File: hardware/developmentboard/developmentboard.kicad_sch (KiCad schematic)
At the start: 38 parts, among them J1 SPI Header, J2 Power Header, J3 Hall Effect Header, U1 ADS7960, U10 DRV5053, U11 DRV5053, U12 DRV5053, U13 DRV5053, U14 AP2138N-2.5, U15 REF5025AD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

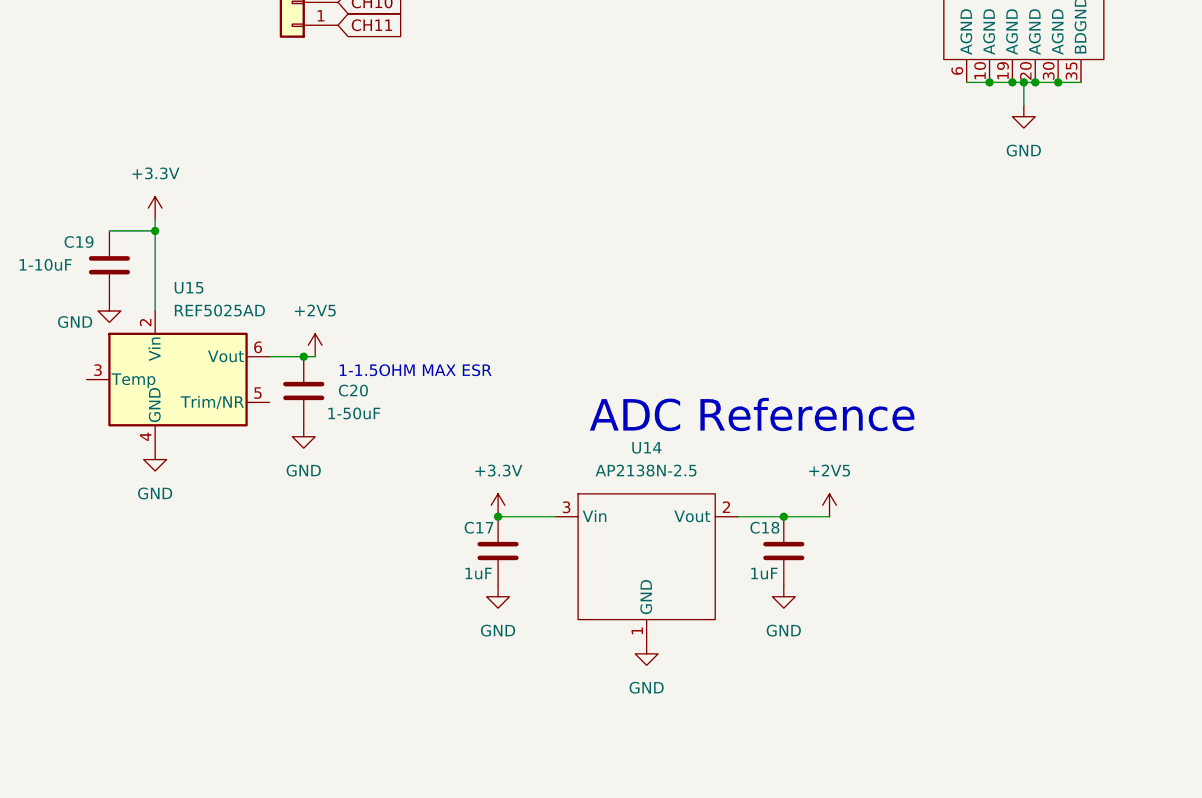
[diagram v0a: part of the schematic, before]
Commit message: added reference IC to PCB, removed LDO
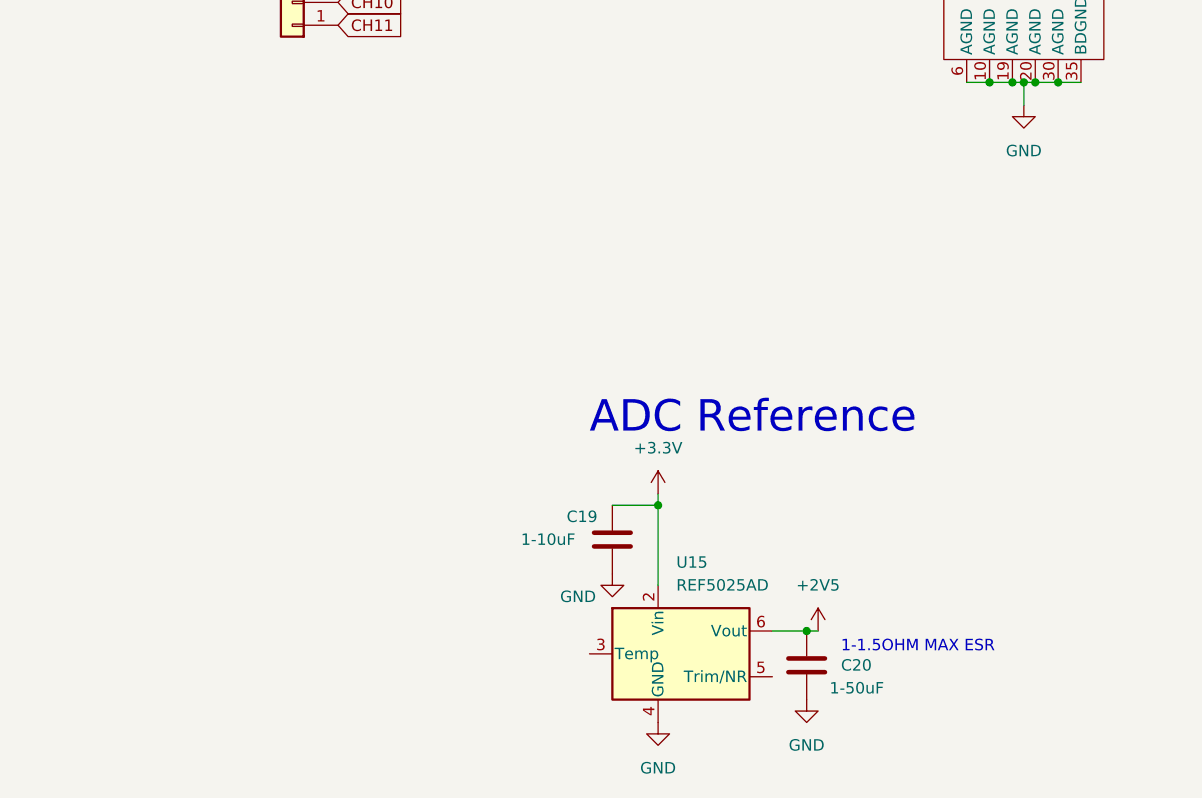
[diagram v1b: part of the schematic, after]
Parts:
- removed C17, C18: 1uF, Capacitor_SMD:C_0603_1608Metric, symbol Device:C
- removed U14: AP2138N-2.5, Package_TO_SOT_SMD:TSOT-23, symbol ece_capstone:AP2138N-2.5
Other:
- moved on the sheet: C19, C20, U15

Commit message: finalized reference IC pcb stuffs - added footprints for bypass caps
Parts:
- C19, C20: footprint (none) -> Capacitor_SMD:C_0603_1608Metric
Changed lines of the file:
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@@
       (effects (font (size 1.27 1.27)) (justify left))
     )
-    (property "Footprint" "" (id 2) (at 108.9152 182.88 0)
+    (property "Footprint" "Capacitor_SMD:C_0603_1608Metric" (id 2) (at 108.9152 182.88 0)
       (effects (font (size 1.27 1.27)) hide)
     )
@@
       (effects (font (size 1.27 1.27)) (justify left))
     )
-    (property "Footprint" "" (id 2) (at 87.3252 168.91 0)
+    (property "Footprint" "Capacitor_SMD:C_0603_1608Metric" (id 2) (at 87.3252 168.91 0)
       (effects (font (size 1.27 1.27)) hide)
     )
@@
     )
     (path "/f6e9c87b-24f6-4288-9254-c44dca53d4ee"
-      (reference "C19") (unit 1) (value "1-10uF") (footprint "")
+      (reference "C19") (unit 1) (value "1-10uF") (footprint "Capacitor_SMD:C_0603_1608Metric")
     )
     (path "/b545a864-3c9e-4894-8a24-dc831b2fea0f"
-      (reference "C20") (unit 1) (value "1-50uF") (footprint "")
+      (reference "C20") (unit 1) (value "1-50uF") (footprint "Capacitor_SMD:C_0603_1608Metric")
     )
     (path "/46e16f3c-0fef-40db-8460-73b8ac70c6ab"

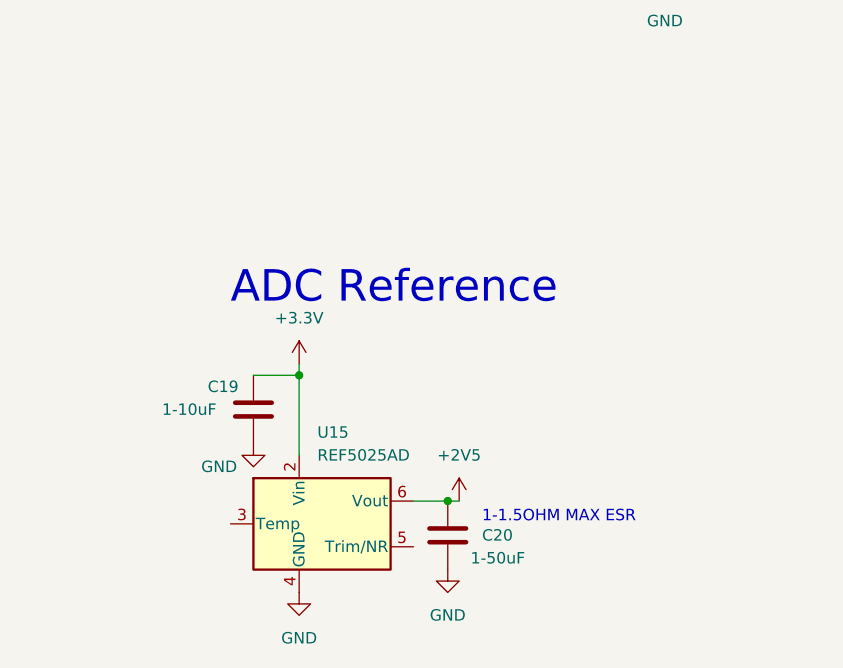
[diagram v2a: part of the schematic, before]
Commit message: made development board wider, changed reference voltage to use shunt regulator
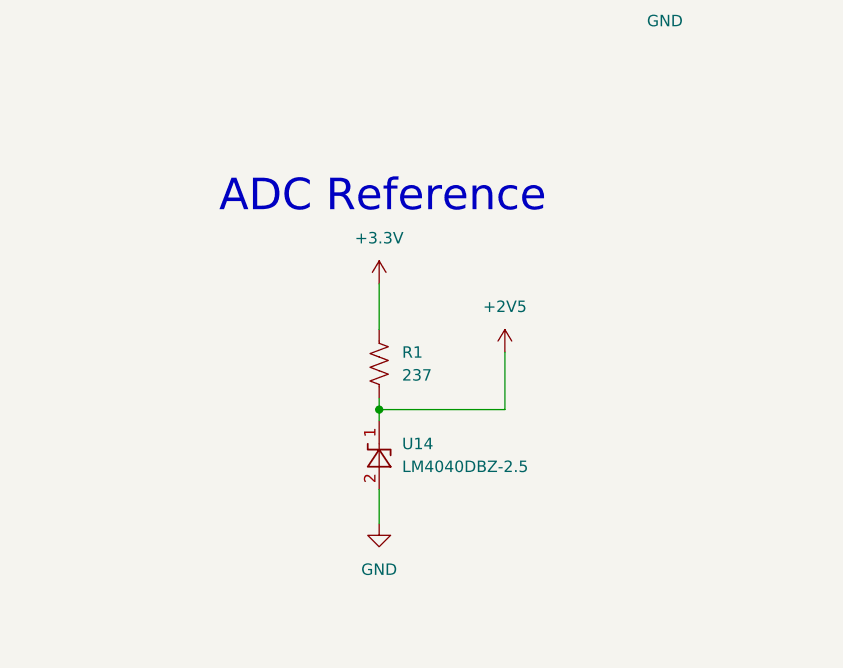
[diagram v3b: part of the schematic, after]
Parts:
- removed C19: 1-10uF, Capacitor_SMD:C_0603_1608Metric, symbol Device:C
- removed C20: 1-50uF, Capacitor_SMD:C_0603_1608Metric, symbol Device:C
- removed U15: REF5025AD, Package_SO:SOIC-8_3.9x4.9mm_P1.27mm, symbol Reference_Voltage:REF5025AD
- added R1: 237, Resistor_SMD:R_1210_3225Metric, symbol Device:R_US
- added U14: LM4040DBZ-2.5, Package_TO_SOT_SMD:SOT-23, symbol Reference_Voltage:LM4040DBZ-2.5
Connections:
- net +2V5: now also R1.2, U14.1 (K)
- net +3.3V: now also R1.1
- net GND: now also U14.2 (A)
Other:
- note removed: "1-1.5OHM MAX ESR"

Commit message: boards board boards no more 3v3 plane and stuwutching
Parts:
- U14: value LM4040DBZ-2.5 -> LM4040CIM3-2.5
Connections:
- net +2V5 renamed 2v5
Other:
- moved on the sheet: R1, U14

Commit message: reworked things on develpoment
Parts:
- removed J1: SPI Header, Connector_PinHeader_2.54mm:PinHeader_1x04_P2.54mm_Vertical, symbol Connector_Generic:Conn_01x04
- removed J2: Power Header, Connector_PinHeader_2.54mm:PinHeader_1x02_P2.54mm_Vertical, symbol Connector_Generic:Conn_01x02
- added H1, H2, H3, H4: MountingHole, MountingHole:MountingHole_4.3mm_M4, symbol Mechanical:MountingHole
- added J1: Conn_01x06_Male, Connector_PinHeader_2.54mm:PinHeader_1x06_P2.54mm_Vertical, symbol Connector:Conn_01x06_Male
- U14: value LM4040CIM3-2.5 -> LM4040DBZ-2.5
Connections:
- net +3.3V: now also J1.5 (Pin_5)
- net CS: now also J1.2 (Pin_2)
- net GND: now also J1.6 (Pin_6)
- net RX: now also J1.4 (Pin_4)
- net SCLK: now also J1.3 (Pin_3)
- net TX: now also J1.1 (Pin_1)
- net 2v5 renamed +2V5
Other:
- note added: "Mounting Points"
- moved on the sheet: R1, U14

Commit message: RP2040 Footprint Reset - See last commit
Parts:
- C1, C10, C11, C12, C14, C15, C16, C2, C3, C4, C5, C6, C7, C8, C9: LCSC (none) -> C90540
- C13: LCSC (none) -> C96446
- J1: value Conn_01x06_Male -> Brain Header; LCSC (none) -> C2932681
- J3: LCSC (none) -> C2833334
- R1: LCSC (none) -> C174455
- U1: LCSC (none) -> C1543353
- U10, U11, U12, U13, U2, U3, U4, U5, U6, U7, U8, U9: LCSC (none) -> C2866569
- U14: LCSC (none) -> C2932681
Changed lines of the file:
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@@
+      (effects (font (size 1.27 1.27)) hide)
+    )
+    (property "LCSC" "C90540" (id 4) (at 236.22 54.61 0)
       (effects (font (size 1.27 1.27)) hide)
     )
@@
       (effects (font (size 1.27 1.27)) hide)
     )
+    (property "LCSC" "C2866569" (id 4) (at 213.36 67.31 0)
+      (effects (font (size 1.27 1.27)) hide)
+    )
     (pin "1")
     (pin "2")
@@
       (effects (font (size 1.27 1.27)) hide)
     )
+    (property "LCSC" "C90540" (id 4) (at 259.08 54.61 0)
+      (effects (font (size 1.27 1.27)) hide)
+    )
     (pin "1")
     (pin "2")
@@
       (effects (font (size 1.27 1.27)) hide)
     )
+    (property "LCSC" "C90540" (id 4) (at 212.09 107.95 0)
+      (effects (font (size 1.27 1.27)) hide)
+    )
     (pin "1")
     (pin "2")
@@
       (effects (font (size 1.27 1.27)) hide)
     )
+    (property "LCSC" "C2866569" (id 4) (at 237.49 93.98 0)
+      (effects (font (size 1.27 1.27)) hide)
+    )
     (pin "1")
     (pin "2")
@@
     )
     (property "part number" "CR1210F237RP05Z" (id 4) (at 128.27 160.02 0)
+      (effects (font (size 1.27 1.27)) hide)
+    )
+    (property "LCSC" "C174455" (id 5) (at 128.27 160.02 0)
       (effects (font (size 1.27 1.27)) hide)
     )
@@
       (effects (font (size 1.27 1.27)) hide)
     )
+    (property "LCSC" "C90540" (id 4) (at 121.92 54.61 0)
+      (effects (font (size 1.27 1.27)) hide)
+    )
     (pin "1")
     (pin "2")
@@
       (effects (font (size 1.27 1.27)) hide)
     )
+    (property "LCSC" "C96446" (id 4) (at 107.95 83.82 0)
+      (effects (font (size 1.27 1.27)) hide)
+    )
     (pin "1")
     (pin "2")
@@
       (effects (font (size 1.27 1.27)) hide)
     )
+    (property "LCSC" "C90540" (id 4) (at 189.23 81.28 0)
+      (effects (font (size 1.27 1.27)) hide)
+    )
     (pin "1")
     (pin "2")
@@
       (effects (font (size 1.27 1.27)) hide)
     )
+    (property "LCSC" "C2866569" (id 4) (at 213.36 40.64 0)
+      (effects (font (size 1.27 1.27)) hide)
+    )
     (pin "1")
     (pin "2")
@@
     (property "Datasheet" "http://www.ti.com/lit/ds/symlink/lm4040-n.pdf" (id 3) (at 128.27 170.18 0)
       (effects (font (size 1.27 1.27) italic) hide)
+    )
+    (property "LCSC" "C2932681" (id 4) (at 128.27 170.18 0)
+      (effects (font (size 1.27 1.27)) hide)
     )
     (pin "1")
@@
       (effects (font (size 1.27 1.27)) hide)
     )
+    (property "LCSC" "C2866569" (id 4) (at 260.35 67.31 0)
+      (effects (font (size 1.27 1.27)) hide)
+    )
     (pin "1")
     (pin "2")
@@
       (effects (font (size 1.27 1.27)) hide)
     )
+    (property "LCSC" "C90540" (id 4) (at 189.23 54.61 0)
+      (effects (font (size 1.27 1.27)) hide)
+    )
     (pin "1")
     (pin "2")
@@
       (effects (font (size 1.27 1.27)) hide)
     )
+    (property "LCSC" "C2866569" (id 4) (at 260.35 93.98 0)
+      (effects (font (size 1.27 1.27)) hide)
+    )
     (pin "1")
     (pin "2")
@@
     )
     (property "Datasheet" "~" (id 3) (at 50.8 95.25 0)
+      (effects (font (size 1.27 1.27)) hide)
+    )
+    (property "LCSC" "C2833334" (id 4) (at 50.8 95.25 0)
       (effects (font (size 1.27 1.27)) hide)
     )
@@
       (effects (font (size 1.27 1.27)) hide)
     )
+    (property "LCSC" "C90540" (id 4) (at 259.08 107.95 0)
+      (effects (font (size 1.27 1.27)) hide)
+    )
     (pin "1")
     (pin "2")
@@
       (effects (font (size 1.27 1.27)) hide)
     )
+    (property "LCSC" "C90540" (id 4) (at 212.09 81.28 0)
+      (effects (font (size 1.27 1.27)) hide)
+    )
     (pin "1")
     (pin "2")
@@
       (effects (font (size 1.27 1.27)) hide)
     )
+    (property "LCSC" "C90540" (id 4) (at 189.23 107.95 0)
+      (effects (font (size 1.27 1.27)) hide)
+    )
     (pin "1")
     (pin "2")
@@
       (effects (font (size 1.27 1.27)) hide)
     )
+    (property "LCSC" "C90540" (id 4) (at 259.08 81.28 0)
+      (effects (font (size 1.27 1.27)) hide)
+    )
     (pin "1")
     (pin "2")
@@
       (effects (font (size 1.27 1.27)) hide)
     )
+    (property "LCSC" "C2866569" (id 4) (at 190.5 67.31 0)
+      (effects (font (size 1.27 1.27)) hide)
+    )
     (pin "1")
     (pin "2")
@@
       (effects (font (size 1.27 1.27)) hide)
     )
+    (property "LCSC" "C2866569" (id 4) (at 237.49 40.64 0)
+      (effects (font (size 1.27 1.27)) hide)
+    )
     (pin "1")
     (pin "2")
@@
       (effects (font (size 1.27 1.27)) hide)
     )
+    (property "LCSC" "C90540" (id 4) (at 124.46 48.26 0)
+      (effects (font (size 1.27 1.27)) hide)
+    )
     (pin "1")
     (pin "2")
@@
       (effects (font (size 1.27 1.27)) hide)
     )
+    (property "LCSC" "C2866569" (id 4) (at 260.35 40.64 0)
+      (effects (font (size 1.27 1.27)) hide)
+    )
     (pin "1")
     (pin "2")
@@
     (in_bom yes) (on_board yes) (fields_autoplaced)
     (property "Reference" "J1" (id 0) (at 45.085 38.1 0))
-    (property "Value" "Conn_01x06_Male" (id 1) (at 45.085 40.64 0))
+    (property "Value" "Brain Header" (id 1) (at 45.085 40.64 0))
     (property "Footprint" "Connector_PinHeader_2.54mm:PinHeader_1x06_P2.54mm_Vertical" (id 2) (at 44.45 48.26 0)
       (effects (font (size 1.27 1.27)) hide)
     )
     (property "Datasheet" "~" (id 3) (at 44.45 48.26 0)
+      (effects (font (size 1.27 1.27)) hide)
+    )
+    (property "LCSC" "C2932681" (id 4) (at 44.45 48.26 0)
       (effects (font (size 1.27 1.27)) hide)
     )
@@
       (effects (font (size 1.27 1.27)) hide)
     )
+    (property "LCSC" "C90540" (id 4) (at 236.22 81.28 0)
+      (effects (font (size 1.27 1.27)) hide)
+    )
     (pin "1")
     (pin "2")
@@
       (effects (font (size 1.27 1.27)) hide)
     )
+    (property "LCSC" "C2866569" (id 4) (at 237.49 67.31 0)
+      (effects (font (size 1.27 1.27)) hide)
+    )
     (pin "1")
     (pin "2")
@@
       (effects (font (size 1.27 1.27)) hide)
     )
+    (property "LCSC" "C90540" (id 4) (at 127 41.91 0)
+      (effects (font (size 1.27 1.27)) hide)
+    )
     (pin "1")
     (pin "2")
@@
       (effects (font (size 1.27 1.27)) hide)
     )
+    (property "LCSC" "C90540" (id 4) (at 212.09 54.61 0)
+      (effects (font (size 1.27 1.27)) hide)
+    )
     (pin "1")
     (pin "2")
@@
       (effects (font (size 1.27 1.27)) hide)
     )
+    (property "LCSC" "C2866569" (id 4) (at 213.36 93.98 0)
+      (effects (font (size 1.27 1.27)) hide)
+    )
     (pin "1")
     (pin "2")
@@
       (effects (font (size 1.27 1.27)) hide)
     )
+    (property "LCSC" "C2866569" (id 4) (at 190.5 93.98 0)
+      (effects (font (size 1.27 1.27)) hide)
+    )
     (pin "1")
     (pin "2")
@@
       (effects (font (size 1.27 1.27)) hide)
     )
+    (property "LCSC" "C90540" (id 4) (at 236.22 107.95 0)
+      (effects (font (size 1.27 1.27)) hide)
+    )
     (pin "1")
     (pin "2")
@@
     )
     (property "Datasheet" "" (id 3) (at 132.08 71.12 0)
+      (effects (font (size 1.27 1.27)) hide)
+    )
+    (property "LCSC" "C1543353" (id 4) (at 132.08 71.12 0)
       (effects (font (size 1.27 1.27)) hide)
     )
@@
       (effects (font (size 1.27 1.27)) hide)
     )
+    (property "LCSC" "C2866569" (id 4) (at 190.5 40.64 0)
+      (effects (font (size 1.27 1.27)) hide)
+    )
     (pin "1")
     (pin "2")
@@
     )
     (path "/bf9d8aae-615a-4e71-9837-820b6960d2a5"
-      (reference "J1") (unit 1) (value "Conn_01x06_Male") (footprint "Connector_PinHeader_2.54mm:PinHeader_1x06_P2.54mm_Vertical")
+      (reference "J1") (unit 1) (value "Brain Header") (footprint "Connector_PinHeader_2.54mm:PinHeader_1x06_P2.54mm_Vertical")
     )
     (path "/6db42d8a-c0b9-4163-8043-8c17d67ff478"

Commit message: Key current and prev values should be setup?
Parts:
- U14: LCSC C2932681 -> C134019
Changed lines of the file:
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@@
       (effects (font (size 1.27 1.27) italic) hide)
     )
-    (property "LCSC" "C2932681" (id 4) (at 128.27 170.18 0)
+    (property "LCSC" "C134019" (id 4) (at 128.27 170.18 0)
       (effects (font (size 1.27 1.27)) hide)
     )

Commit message: Rev.2 Boards Headers updated Male on Keysboard, Female on Brainboard
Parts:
- J1: LCSC C2932681 -> C492414
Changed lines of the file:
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@@
       (effects (font (size 1.27 1.27)) hide)
     )
-    (property "LCSC" "C2932681" (id 4) (at 44.45 48.26 0)
+    (property "LCSC" "C492414" (id 4) (at 44.45 48.26 0)
       (effects (font (size 1.27 1.27)) hide)
     )
